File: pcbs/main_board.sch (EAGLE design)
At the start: 62 parts, among them IC1 317T, IC2 MEGA48/88/168-AU, J1 22-27-2021-02, K1 G6K-2F, Q1 MOSFET-NCHANNELSMD, Q2 MOSFET-NCHANNELSMD

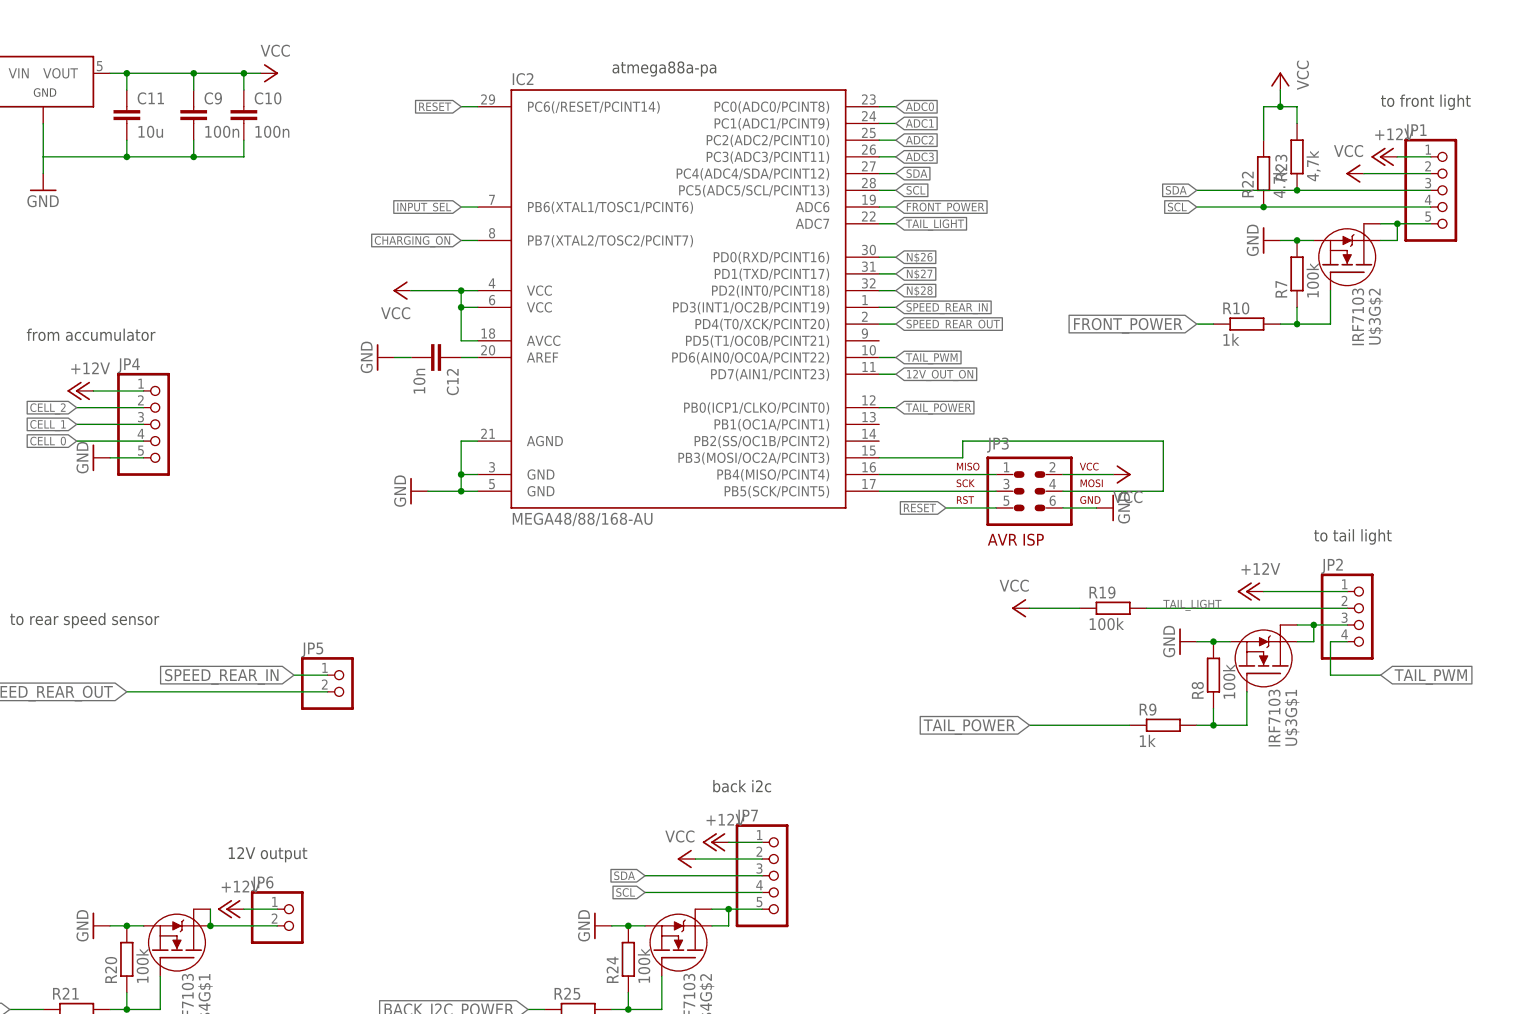
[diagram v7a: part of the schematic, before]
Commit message: Main Board: Started layouting control part
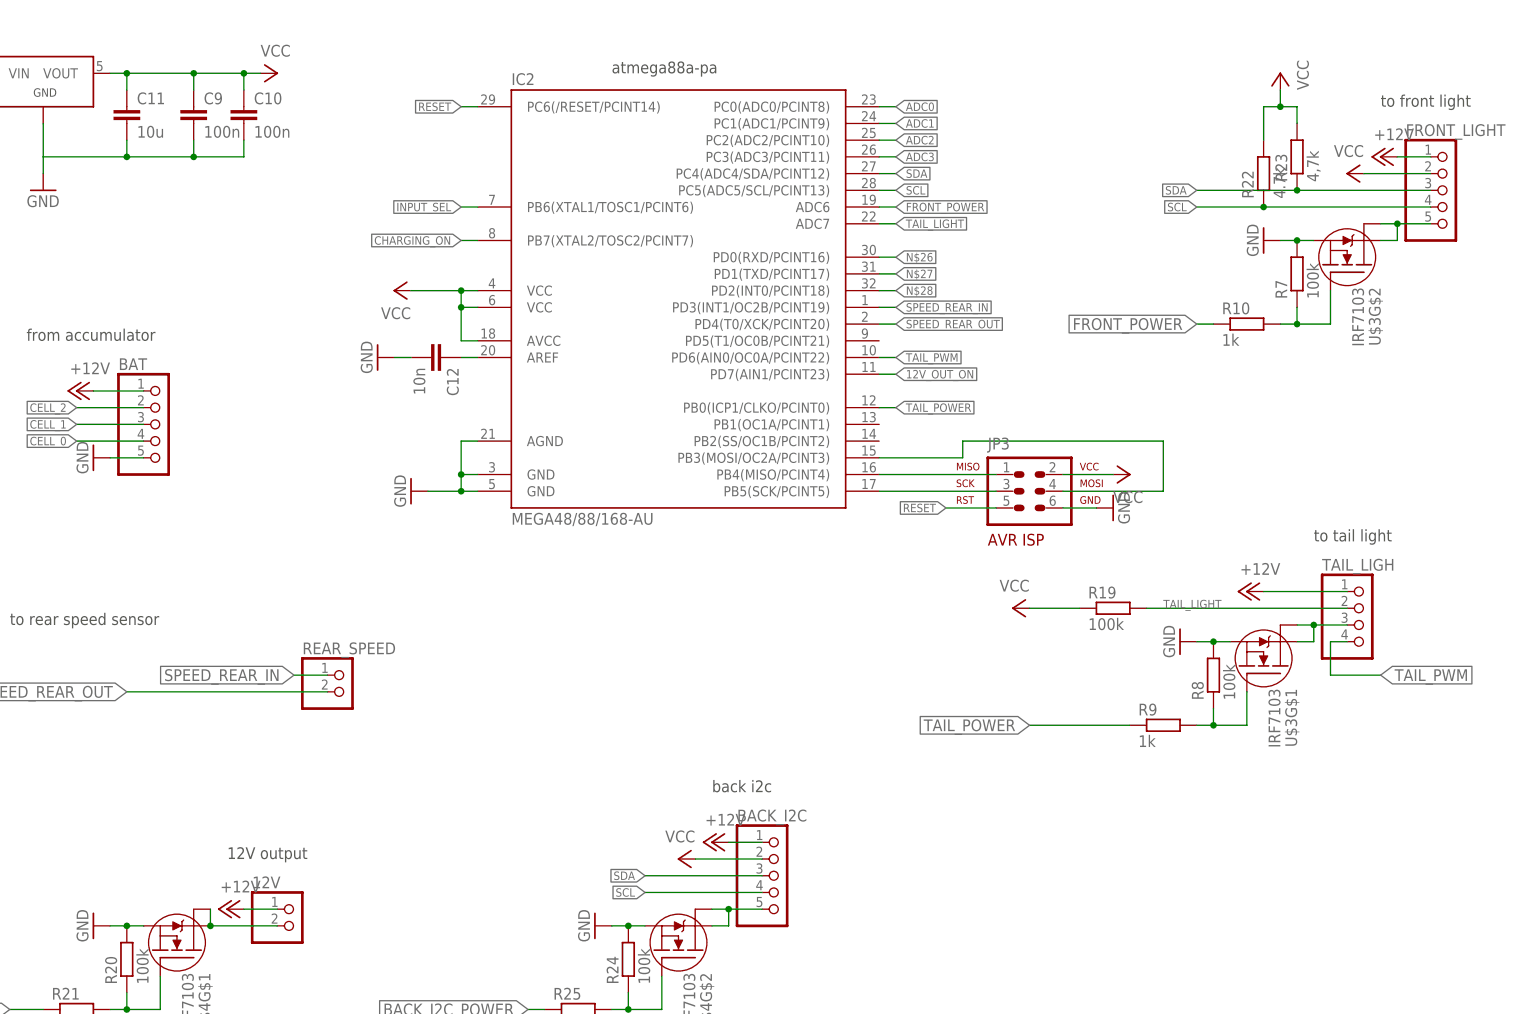
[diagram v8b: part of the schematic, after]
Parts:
- renumbered JP1 to FRONT_LIGHT, JP2 to TAIL_LIGH, JP4 to BAT, JP5 to REAR_SPEED, JP6 to 12V, JP7 to BACK_I2C
